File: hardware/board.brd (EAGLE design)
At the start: 53 x 30 mm, 47 parts, among them IC1 0915BM15A0001, J1 U.FL, U2 TPS63030DSKT, U3 BLE113-A, X1 CTS_32X25_SMD, X3 MINI-USB-UX60-MB-5ST

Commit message: Fix coverter part number
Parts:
- U2: value TPS63030DSKT -> TPS63031
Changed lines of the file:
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@@
 <element name="U$2" library="parts" package="PTS540" value="TACTILE_SWITCH" x="30.655" y="16.735" rot="R270"/>
 <element name="U1" library="parts" package="5PIN_SOT23" value="" x="6.86" y="16.33"/>
-<element name="U2" library="Texas Instruments_By_element14_Batch_1" package="SON50P260X260X80-11N" value="TPS63030DSKT" x="31.5" y="23" rot="R90">
+<element name="U2" library="Texas Instruments_By_element14_Batch_1" package="SON50P260X260X80-11N" value="TPS63031" x="31.5" y="23" rot="R90">
 <attribute name="PACKAGE" value="SON-10" x="31.5" y="23" size="1.778" layer="27" rot="R90" display="off"/>
 <attribute name="OC_NEWARK" value="19P7478" x="31.5" y="23" size="1.778" layer="27" rot="R90" display="off"/>
-<attribute name="MPN" value="TPS63030DSKT" x="31.5" y="23" size="1.778" layer="27" rot="R90" display="off"/>
+<attribute name="MPN" value="TPS63031" x="31.5" y="23" size="1.778" layer="27" rot="R90" display="off"/>
 <attribute name="SUPPLIER" value="Texas Instruments" x="31.5" y="23" size="1.778" layer="27" rot="R90" display="off"/>
 <attribute name="OC_FARNELL" value="1686303" x="31.5" y="23" size="1.778" layer="27" rot="R90" display="off"/>

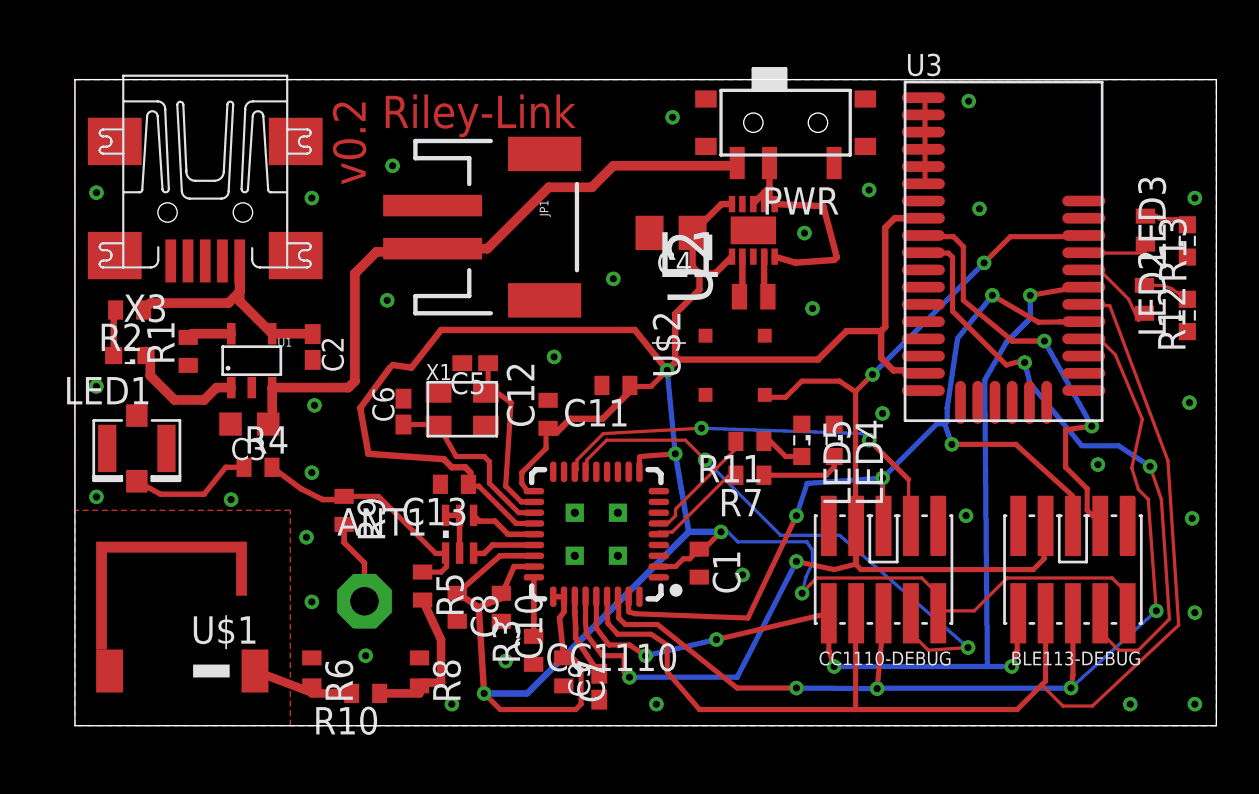
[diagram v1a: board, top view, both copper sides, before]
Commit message: Remove chip antenna, add fiducials, clean up labels, annotate RileyLink0.3
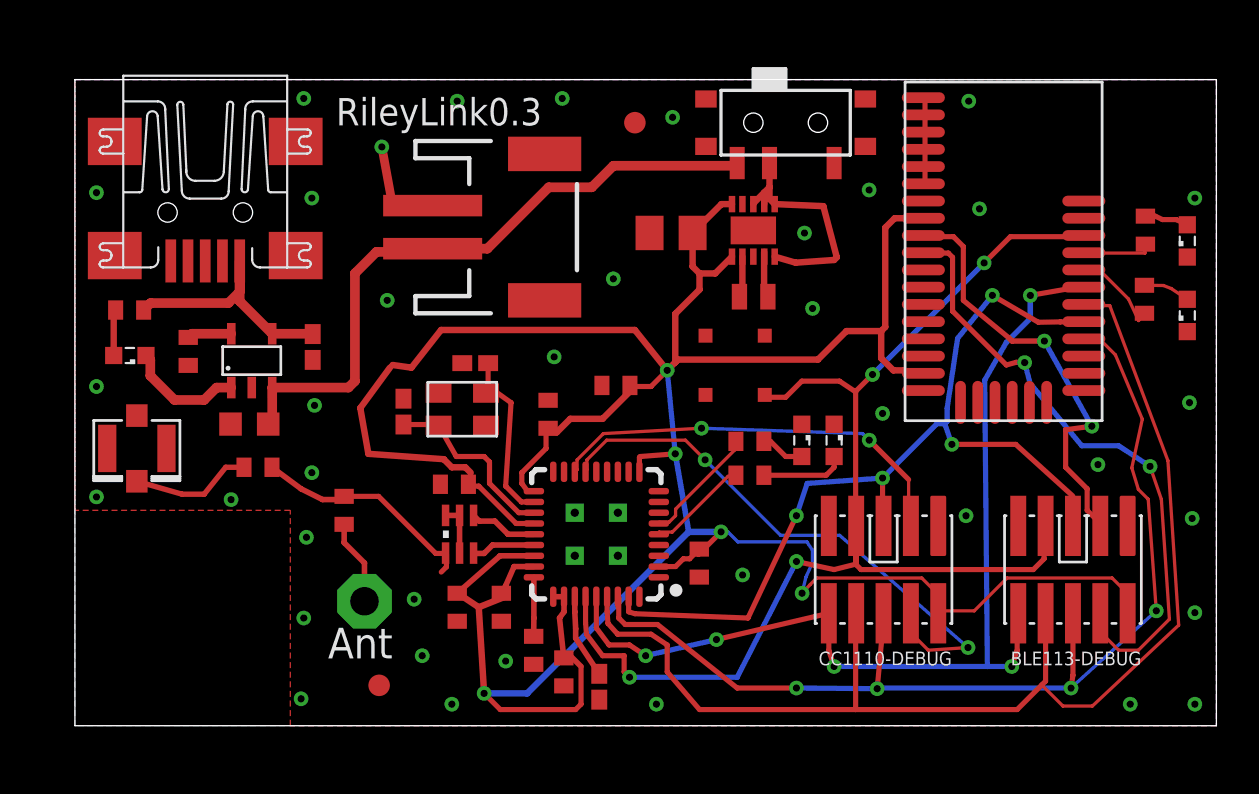
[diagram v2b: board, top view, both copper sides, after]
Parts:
- removed R10, R5, R6, R8: (no value), rcl:R0402
- added U$3: FIDUCIAL, adafruit:FIDUCIAL_1MM
- U$1: value 915_ANT -> FIDUCIAL; device parts:915_ANT -> adafruit:FIDUCIAL_1MM
- moved U$1 8.17 mm to (14.1, 1.88), turned to 0 degrees
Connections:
- removed net N$11: R10.1, R5.2, R8.2
- removed net N$13: R10.2, R6.2, U$1.P$1
- net GND: no longer R6.1, R8.1
- net N$10: no longer R5.1
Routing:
- net N$11: track 7.29 -> 0.00 mm
- net N$13: track 5.33 -> 0.00 mm
- net GND: track 7.00 -> 11.6 mm, vias 33 -> 38
- net N$10: track 11.5 -> 10.7 mm
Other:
- board text added: "Ant"
- board text added: "RileyLink0.3"
- board text removed: "Riley-Link"
- board text removed: "v0.2"

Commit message: Rounded corners, align fiducials
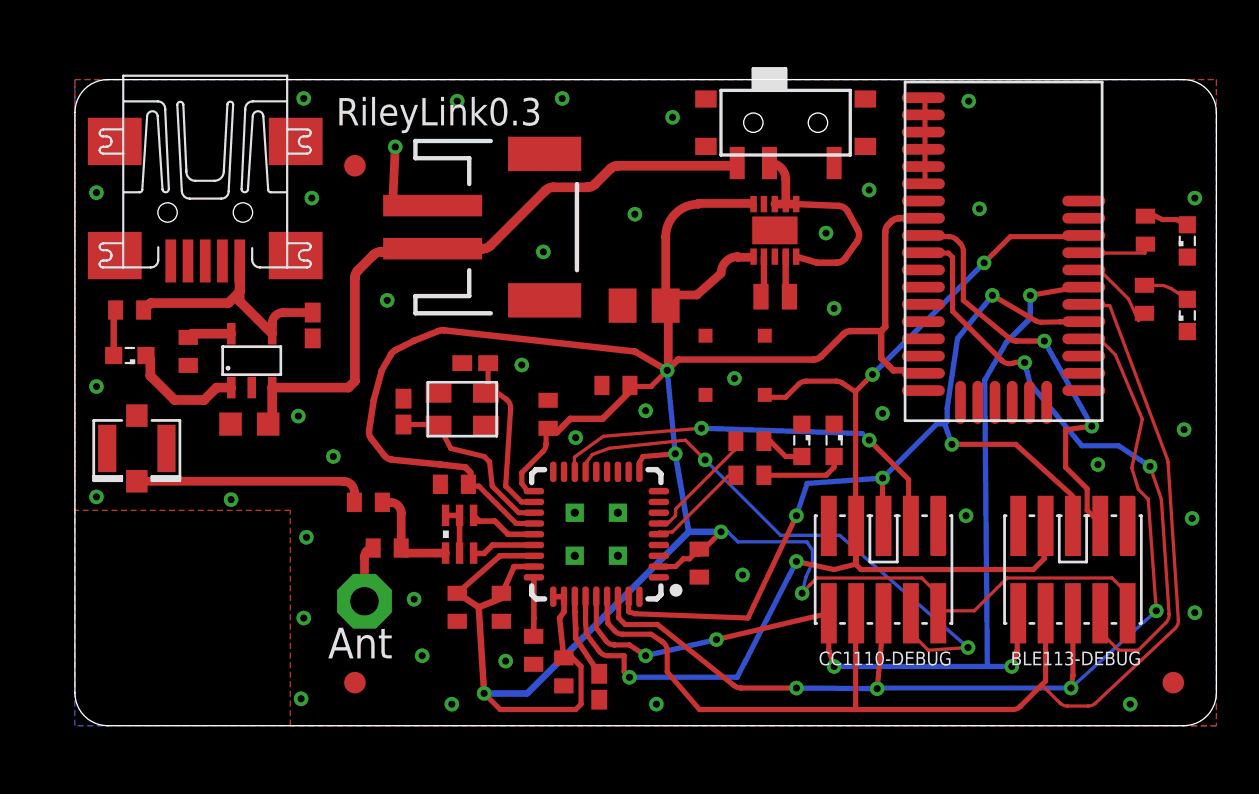
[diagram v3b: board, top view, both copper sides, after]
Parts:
- removed U$1, U$3: FIDUCIAL, adafruit:FIDUCIAL_1MM
- removed U2: TPS63031, Texas Instruments_By_element14_Batch_1:SON50P260X260X80-11N
- added FID1, FID2, FID3: FIDUCIAL, adafruit:FIDUCIAL_1MM
- added REGULATOR: TPS63031, Texas Instruments_By_element14_Batch_1:SON50P260X260X80-11N
- moved R4 5.38 mm to (13.6, 10.4)
- moved C4 3.60 mm to (26.4, 19.5)
- moved R9 2.66 mm to (14.5, 8.25), turned to 180 degrees
- moved C2 1.00 mm to (11.0, 18.6)
- moved L1 1.00 mm to (32.5, 19.9)
- renumbered U1 to CHARGER
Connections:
- net GND: now also REGULATOR.11, REGULATOR.3, REGULATOR.9; no longer U2.11, U2.3, U2.9
- net N$1: now also REGULATOR.2; no longer U2.2
- net N$6: now also REGULATOR.4; no longer U2.4
- net V+: now also REGULATOR.5, REGULATOR.6, REGULATOR.7, REGULATOR.8; no longer U2.5, U2.6, U2.7, U2.8
- net VDD: now also REGULATOR.1, REGULATOR.10; no longer U2.1, U2.10
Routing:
- net N$10: track 10.7 -> 4.94 mm
- net N$9: track 5.66 -> 10.8 mm
- net VDD: track 149.1 -> 152.6 mm
- net N$12: track 3.96 -> 2.64 mm
- net V+: track 11.3 -> 10.5 mm
- net VIN_USB: track 12.1 -> 12.8 mm
- net GND: vias 38 -> 41
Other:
- outline, holes or cut-outs redrawn
